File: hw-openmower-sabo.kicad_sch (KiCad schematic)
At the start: 25 parts, among them J1 Conn_01x05_Pin, J20 Conn_01x02, J31 Conn_01x03_Pin, J32 Conn_02x08_Odd_Even, J33 Molex 470531000, M1 Fan, M2 Fan, Q4 BSS138, Q5 BSS138, U44 INA180A1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

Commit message: v0.3 prototype
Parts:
- C88: value 100nF@50V -> 100nF
- J31: now not fitted; now left out of the parts list
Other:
- sheet RobotConnectors ports: added I2C4_ID{SDA SCL}, SEL_SPI_MISO_~{UI_S2}/BMC, SEL_SPI_MOSI_~{UI_S2}/LCD, SPI_MISO, SPI_MOSI, UI_S2_BTN_SH/~{LD}, UI_S2_STR; removed INP_~{CS}, LATCH_~{LOAD}, SPI_RX, SPI_TX, UI_S2_BTN_~{CS}, ~{OE}
- note added: "I2C Addr (7-Bit) = 0x50"
- note removed: "----- REQUIRED REWORK ----- 1. See RobotConnectors"
- note removed: "<--| MODed to be UI_S2_~{LOAD}"
- note removed: "MODed to be <--- UI_S2_LATCH"

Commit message: BOM optimization
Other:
- title: OpenMower SABO Mainboard for Series I & II -> OpenMower SABO Carrierboard for Series I & II
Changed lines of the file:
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@@
 	(paper "A3")
 	(title_block
-		(title "OpenMower SABO Mainboard for Series I & II")
-		(date "2025-10-05")
-		(rev "v0.3")
+		(title "OpenMower SABO Carrierboard for Series I & II")
+		(date "2025-10-12")
+		(rev "v0.4")
 		(company "Apeheanger <joerg@ebeling.ws> for OpenMower")
 		(comment 1 "This design is licensed under CC BY-NC 4.0")
@@
 			)
 		)
-		(property "Description" "Unpolarized capacitor"
+		(property "Description" "50V 100nF X7R ±10% 0402 Multilayer Ceramic Capacitors MLCC"
 			(at 228.6 241.3 0)
 			(effects
@@
 			)
 		)
-		(property "Description" "Unpolarized capacitor"
+		(property "Description" "50V 100nF X7R ±10% 0402 Multilayer Ceramic Capacitors MLCC"
 			(at 25.4 31.75 0)
 			(effects

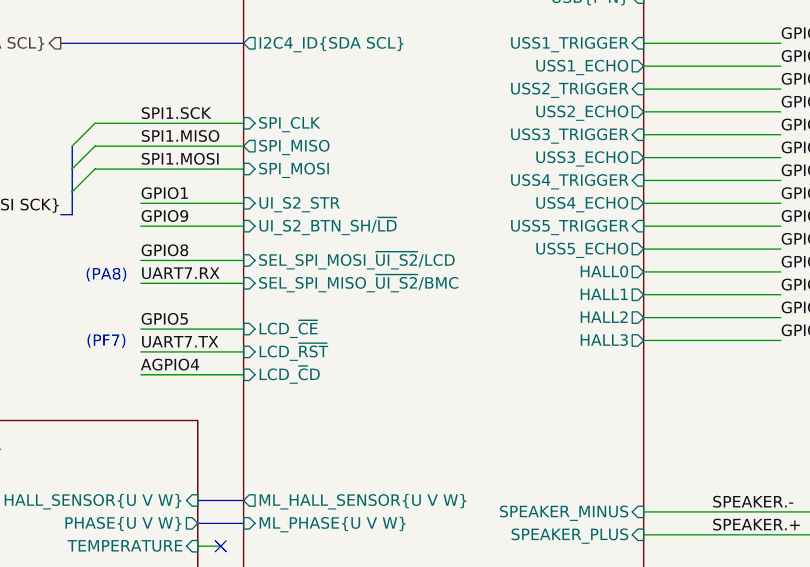
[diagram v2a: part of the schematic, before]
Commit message: Typo BMC to BMS
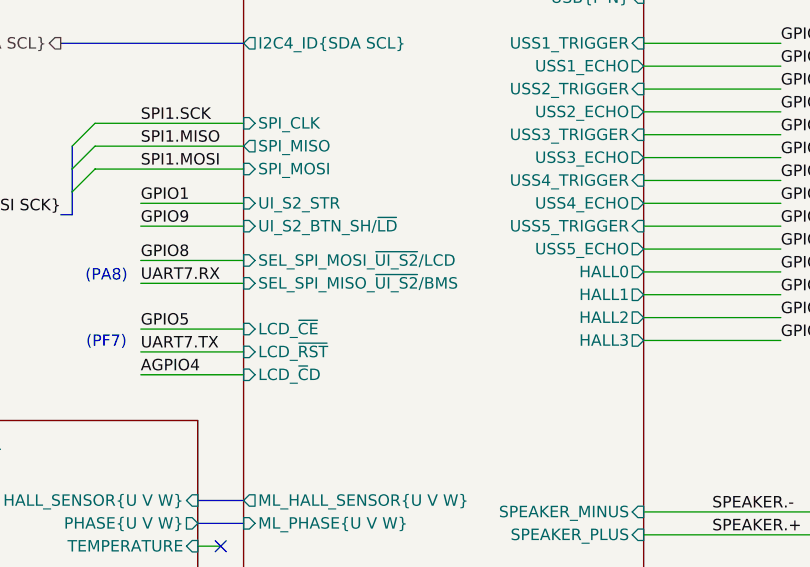
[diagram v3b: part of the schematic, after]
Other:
- sheet RobotConnectors ports: added SEL_SPI_MISO_~{UI_S2}/BMS; removed SEL_SPI_MISO_~{UI_S2}/BMC
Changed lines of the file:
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@@
 			)
 		)
-		(pin "SEL_SPI_MISO_~{UI_S2}{slash}BMC" input
+		(pin "SEL_SPI_MISO_~{UI_S2}{slash}BMS" input
 			(at 72.39 171.45 180)
 			(effects

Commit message: Add latest findings
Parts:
- removed R37: 27k, Resistor_SMD:R_0603_1608Metric_Pad0.98x0.95mm_HandSolder, symbol Device:R
- removed R38: 22k, Resistor_SMD:R_0603_1608Metric_Pad0.98x0.95mm_HandSolder, symbol Device:R
- added C96: 100nF, Capacitor_SMD:C_0603_1608Metric, symbol Device:C
- added R9: 10k, Resistor_SMD:R_0603_1608Metric_Pad0.98x0.95mm_HandSolder, symbol Device:R
- J31: now fitted; now in the parts list
- R36: value 0.1 -> 0.05; footprint Resistor_SMD:R_1206_3216Metric -> Resistor_SMD:R_2512_6332Metric; JLC C188071 -> C459687
- U44: value INA180A1 -> INA293A1; symbol Amplifier_Current:INA180A1 -> Amplifier_Current:INA293A1; JLC (none) -> C1855804; LCSC Part # C122228 -> (none)
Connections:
- net AGPIO2: now also C96.1, R9.2; no longer U44.1
- net GND: now also C96.2
- net at U44.3 (IN+): now also D15.1 (K), D28.1 (K), R36.1
- new net: R9.1, U44.1 (OUT)
- no-connect marks 9 -> 12
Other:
- sheet Connectors ports: added none; removed ETH1{ETH_TPI}
- sheet RobotConnectors ports: added I2C_BMS{SDA SCL}, I2C_GPIO{SDA SCL}; removed BATTERY_CHARGE_INPUT, I2C4_ID{SDA SCL}, SEL_SPI_MISO_~{UI_S2}/BMS, SEL_SPI_MOSI_~{UI_S2}/LCD
- note added: "Unused GPIOs"
- note added: "τ = 10kΩ*100nF = 1 ms 99% = 5τ = 5 ms"
- moved on the sheet: C88, R36

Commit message: Prepare for next production - Slightly adapt part selection - Add TC2050 holes
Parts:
- C63, C88: JLC C307331 -> (none); LCSC Part # (none) -> C307331
- C96: JLC C14663 -> (none); LCSC Part # (none) -> C14663
- D15, D28: JLC C22452 -> (none); LCSC Part # (none) -> C22452
- D22, D25: JLC C8598 -> (none); LCSC Part # (none) -> C8598
- J1: JLC C6332198 -> (none)
- J20: JLC C98734 -> (none)
- J31: JLC C6332196 -> (none); LCSC Part # (none) -> C6332196
- J32: JLC C5383108 -> (none); LCSC Part # (none) -> C5383108
- J33: JLC C2761402 -> (none); LCSC Part # (none) -> C2761402
- M1, M2: JLC C2935908 -> (none); LCSC Part # (none) -> C2935908
- Q4, Q5: JLC C3040446 -> (none); LCSC Part # (none) -> C3040446
- R31: JLC C25744 -> (none); LCSC Part # (none) -> C25744
- R36: JLC C459687 -> (none); LCSC Part # (none) -> C459687
- R52, R60: JLC C17414 -> (none); LCSC Part # (none) -> C17414
- R53, R65: JLC C17471 -> (none); LCSC Part # (none) -> C17471
- R9: JLC C25804 -> (none); LCSC Part # (none) -> C25804
- U44: JLC C1855804 -> (none); LCSC Part # (none) -> C1855804

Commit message: Next proto prep
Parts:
- Q4, Q5: value BSS138 -> AO3400A; LCSC Part # C3040446 -> C20917
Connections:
- no-connect marks 12 -> 10
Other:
- sheet RobotConnectors ports: added UI_S1_~{CON}, UI_S2_~{CON}; removed none
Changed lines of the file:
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@@
 	(text "(PA8)"
 		(exclude_from_sim no)
-		(at 30.734 89.154 0)
+		(at 66.294 167.894 0)
 		(effects
 			(font
@@
 	)
 	(no_connect
-		(at 40.64 93.98)
-	)
-	(no_connect
-		(at 40.64 90.17)
-	)
-	(no_connect
 		(at 191.77 63.5)
 	)
@@
 	(wire
 		(pts
-			(xy 17.78 93.98) (xy 40.64 93.98)
-		)
-		(stroke
-			(width 0)
-			(type default)
-		)
-	)
-	(wire
-		(pts
 			(xy 124.46 241.3) (xy 124.46 242.57)
 		)
@@
 	(wire
 		(pts
-			(xy 17.78 90.17) (xy 40.64 90.17)
-		)
-		(stroke
-			(width 0)
-			(type default)
-		)
-	)
-	(wire
-		(pts
 			(xy 297.18 83.82) (xy 297.18 85.09)
 		)
@@
 	(wire
 		(pts
+			(xy 53.34 171.45) (xy 72.39 171.45)
+		)
+		(stroke
+			(width 0)
+			(type default)
+		)
+	)
+	(wire
+		(pts
 			(xy 334.01 147.32) (xy 349.25 147.32)
 		)
@@
 	(wire
 		(pts
+			(xy 53.34 168.91) (xy 72.39 168.91)
+		)
+		(stroke
+			(width 0)
+			(type default)
+		)
+	)
+	(wire
+		(pts
 			(xy 189.23 229.87) (xy 195.58 229.87)
 		)
@@
 	)
 	(label "UART7.RX"
-		(at 17.78 90.17 0)
+		(at 53.34 168.91 0)
 		(effects
 			(font
@@
 	)
 	(label "GPIO8"
-		(at 17.78 93.98 0)
+		(at 53.34 171.45 0)
 		(effects
 			(font
@@
 			)
 		)
-		(property "Value" "BSS138"
+		(property "Value" "AO3400A"
 			(at 355.6 91.4399 0)
 			(effects
@@
 			)
 		)
-		(property "Description" "50V Vds, 0.22A Id, N-Channel MOSFET, SOT-23"
+		(property "Description" "-55℃~+150℃ 1 N-channel 1.45V 1.4W 30V 48mΩ@2.5V 5.7A 50pF 630pF 75pF 7nC@10V N-Channel SOT-23-3L MOSFETs ROHS"
 			(at 349.25 90.17 0)
 			(effects
@@
 			)
 		)
-		(property "LCSC Part #" "C3040446"
+		(property "LCSC Part #" "C20917"
 			(at 349.25 90.17 0)
 			(effects
@@
 			)
 		)
-		(property "Value" "BSS138"
+		(property "Value" "AO3400A"
 			(at 300.99 91.4399 0)
 			(effects
@@
 			)
 		)
-		(property "Description" "50V Vds, 0.22A Id, N-Channel MOSFET, SOT-23"
+		(property "Description" "-55℃~+150℃ 1 N-channel 1.45V 1.4W 30V 48mΩ@2.5V 5.7A 50pF 630pF 75pF 7nC@10V N-Channel SOT-23-3L MOSFETs ROHS"
 			(at 294.64 90.17 0)
 			(effects
@@
 			)
 		)
-		(property "LCSC Part #" "C3040446"
+		(property "LCSC Part #" "C20917"
 			(at 294.64 90.17 0)
 			(effects
@@
 			(effects
 				(font
+					(size 1.27 1.27)
+				)
+				(justify left)
+			)
+		)
+		(pin "UI_S1_~{CON}" input
+			(at 72.39 168.91 180)
+			(effects
+				(font
+					(size 1.27 1.27)
+				)
+				(justify left)
+			)
+		)
+		(pin "UI_S2_~{CON}" input
+			(at 72.39 171.45 180)
+			(effects
+				(font

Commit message: Production state
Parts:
- added J19: Conn_01x02, Connector_JST:JST_XH_B2B-XH-A_1x02_P2.50mm_Vertical, symbol Connector_Generic:Conn_01x02
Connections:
- net Charger/NTC_BATT: now also J19.1 (Pin_1)
- net GND: now also J19.2 (Pin_2)
- no-connect marks 10 -> 9
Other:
- note added: "Unused GPIOs: None ATM"
- note removed: "Unused GPIOs"
